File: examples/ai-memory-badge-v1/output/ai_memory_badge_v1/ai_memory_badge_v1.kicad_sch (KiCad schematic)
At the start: 0 parts

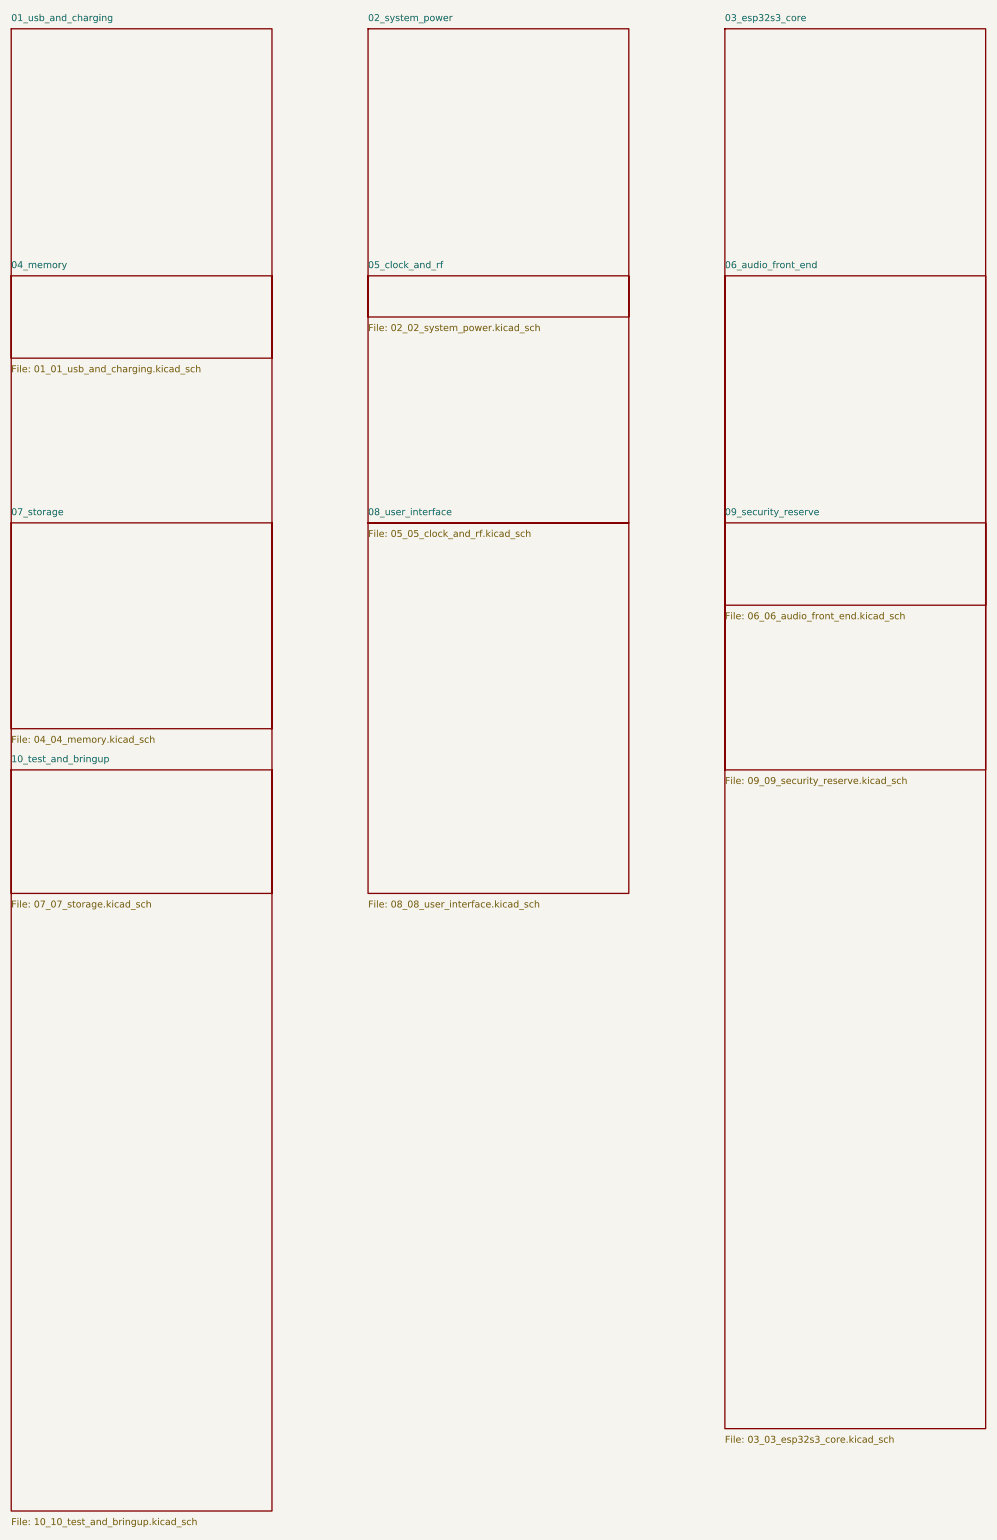
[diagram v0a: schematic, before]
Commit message: feat: split schematic layout from PCB placement / 将原理图布局与PCB摆位分离
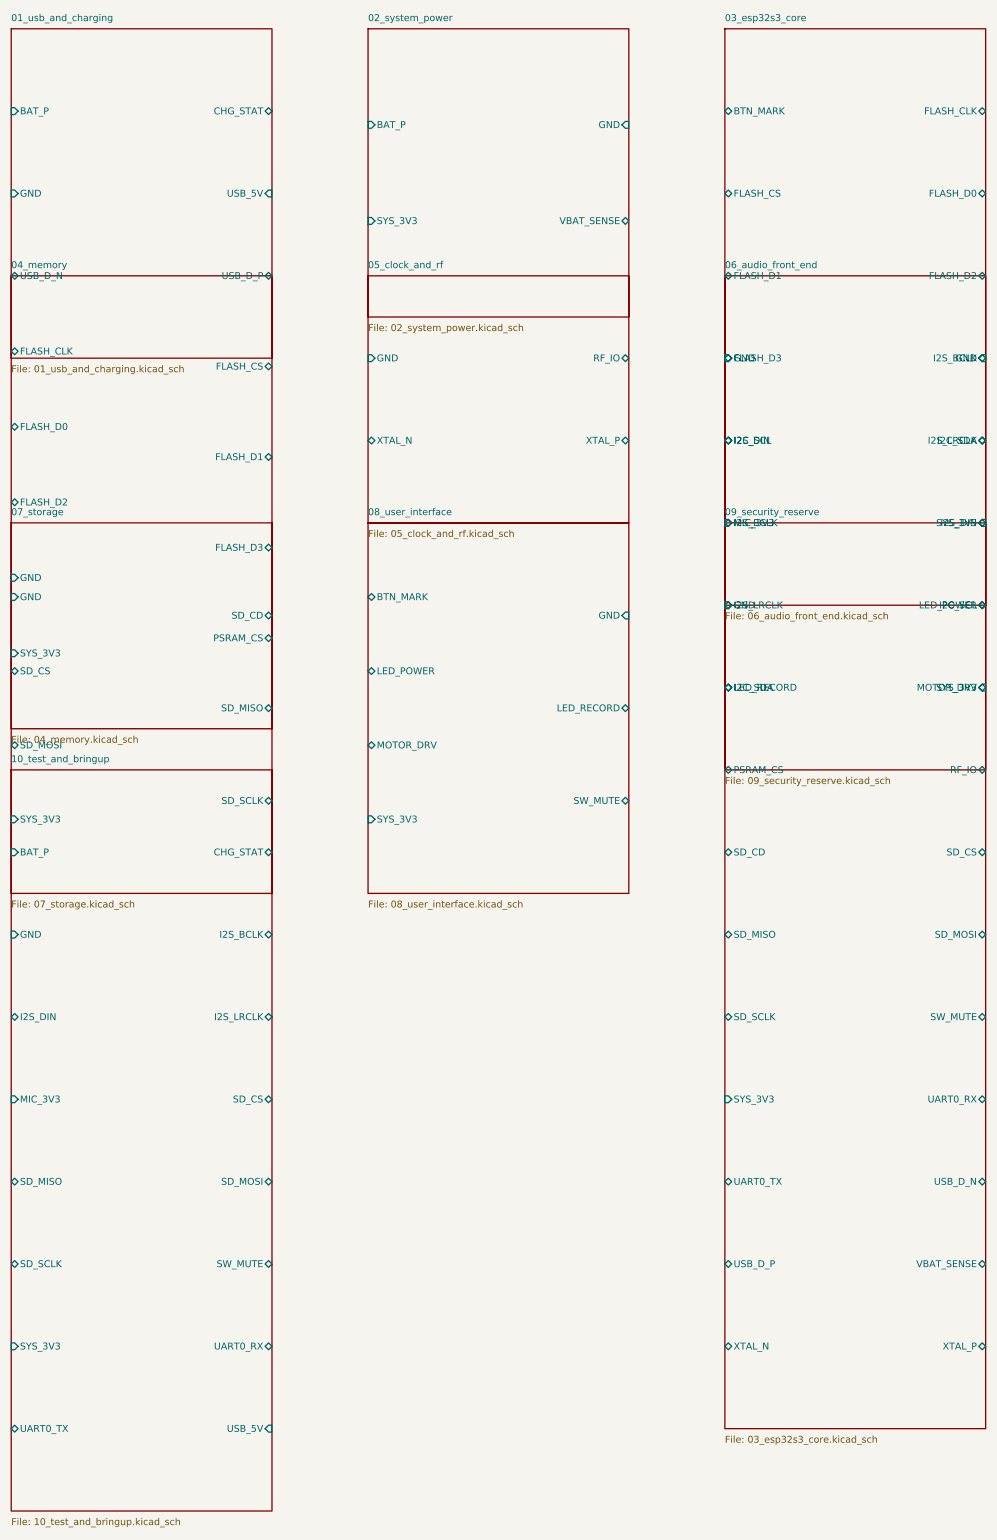
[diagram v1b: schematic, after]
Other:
- sheet 01_usb_and_charging: file 01_01_usb_and_charging.kicad_sch -> 01_usb_and_charging.kicad_sch
- sheet 01_usb_and_charging ports: added BAT_P, CHG_STAT, GND, USB_5V, USB_D_N, USB_D_P; removed none
- sheet 02_system_power: file 02_02_system_power.kicad_sch -> 02_system_power.kicad_sch
- sheet 02_system_power ports: added BAT_P, GND, SYS_3V3, VBAT_SENSE; removed none
- sheet 03_esp32s3_core: file 03_03_esp32s3_core.kicad_sch -> 03_esp32s3_core.kicad_sch
- sheet 03_esp32s3_core ports: added BTN_MARK, FLASH_CLK, FLASH_CS, FLASH_D0, FLASH_D1, FLASH_D2, FLASH_D3, GND, I2C_SCL, I2C_SDA, I2S_BCLK, I2S_DIN, I2S_LRCLK, LED_POWER, LED_RECORD, MOTOR_DRV, PSRAM_CS, RF_IO, SD_CD, SD_CS, SD_MISO, SD_MOSI, SD_SCLK, SW_MUTE, SYS_3V3, UART0_RX, UART0_TX, USB_D_N, USB_D_P, VBAT_SENSE, XTAL_N, XTAL_P; removed none
- sheet 04_memory: file 04_04_memory.kicad_sch -> 04_memory.kicad_sch
- sheet 04_memory ports: added FLASH_CLK, FLASH_CS, FLASH_D0, FLASH_D1, FLASH_D2, FLASH_D3, GND, PSRAM_CS, SYS_3V3; removed none
- sheet 05_clock_and_rf: file 05_05_clock_and_rf.kicad_sch -> 05_clock_and_rf.kicad_sch
- sheet 05_clock_and_rf ports: added GND, RF_IO, XTAL_N, XTAL_P; removed none
- sheet 06_audio_front_end: file 06_06_audio_front_end.kicad_sch -> 06_audio_front_end.kicad_sch
- sheet 06_audio_front_end ports: added GND, I2S_BCLK, I2S_DIN, I2S_LRCLK, MIC_3V3, SYS_3V3; removed none
- sheet 07_storage: file 07_07_storage.kicad_sch -> 07_storage.kicad_sch
- sheet 07_storage ports: added GND, SD_CD, SD_CS, SD_MISO, SD_MOSI, SD_SCLK, SYS_3V3; removed none
- sheet 08_user_interface: file 08_08_user_interface.kicad_sch -> 08_user_interface.kicad_sch
- sheet 08_user_interface ports: added BTN_MARK, GND, LED_POWER, LED_RECORD, MOTOR_DRV, SW_MUTE, SYS_3V3; removed none
- sheet 09_security_reserve: file 09_09_security_reserve.kicad_sch -> 09_security_reserve.kicad_sch
- sheet 09_security_reserve ports: added GND, I2C_SCL, I2C_SDA, SYS_3V3; removed none
- sheet 10_test_and_bringup: file 10_10_test_and_bringup.kicad_sch -> 10_test_and_bringup.kicad_sch
- sheet 10_test_and_bringup ports: added BAT_P, CHG_STAT, GND, I2S_BCLK, I2S_DIN, I2S_LRCLK, MIC_3V3, SD_CS, SD_MISO, SD_MOSI, SD_SCLK, SW_MUTE, SYS_3V3, UART0_RX, UART0_TX, USB_5V; removed none
